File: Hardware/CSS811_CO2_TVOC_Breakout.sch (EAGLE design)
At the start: 19 parts, among them U2 CCS811PRODUCTION

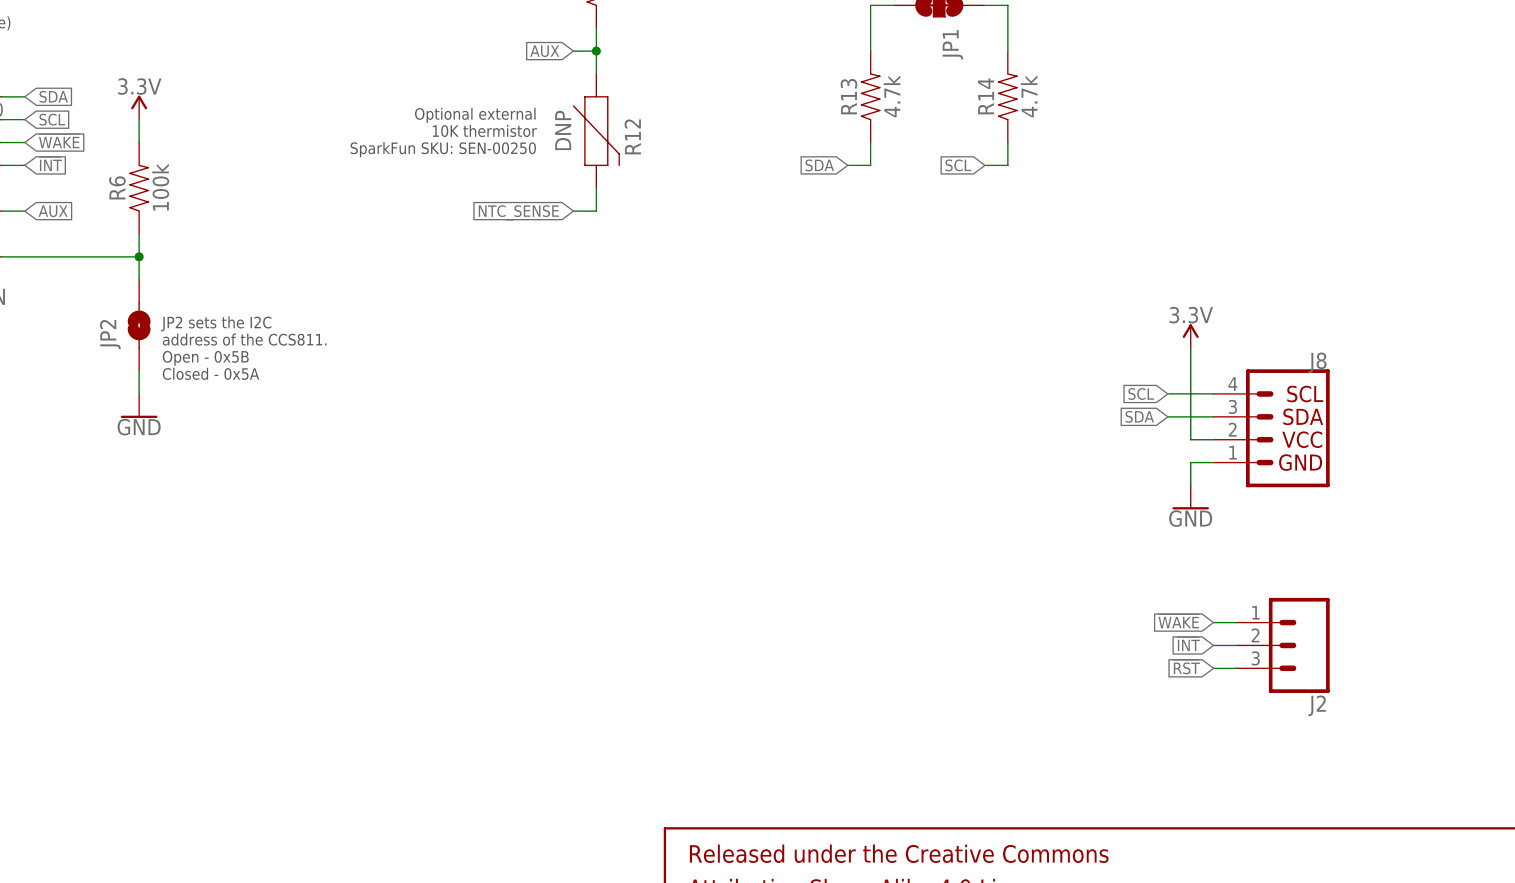
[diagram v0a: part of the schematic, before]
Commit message: Adding panel and removing extraneous files.
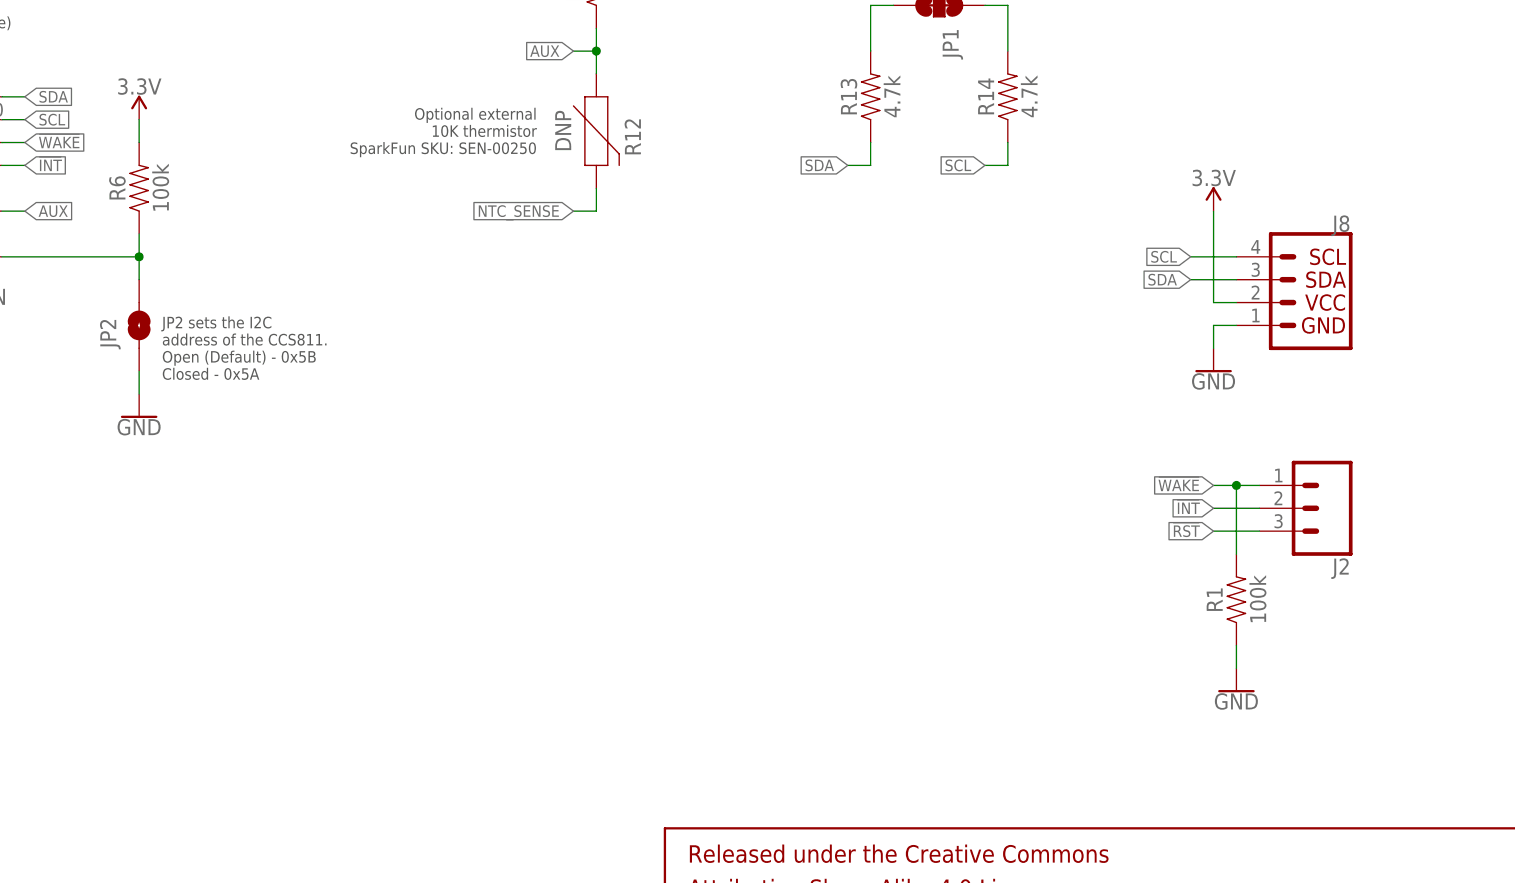
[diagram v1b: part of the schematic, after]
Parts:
- added R1: 100k, SparkFun-Resistors:100KOHM-0603-1/10W-1%
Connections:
- net !WAKE: now also R1.2
- net GND: now also R1.1
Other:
- note added: "JP2 sets the I2C address of the CCS811. Open (Default) - 0x5B Closed - 0x5A"
- note removed: "JP2 sets the I2C address of the CCS811. Open - 0x5B Closed - 0x5A"
- moved on the sheet: J2, J8
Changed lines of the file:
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@@
 <?xml version="1.0" encoding="utf-8"?>
 <!DOCTYPE eagle SYSTEM "eagle.dtd">
-<eagle version="7.5.0">
+<eagle version="7.7.0">
 <drawing>
 <settings>
@@
 <part name="J2" library="SparkFun-Connectors" deviceset="CONN_03" device="1X03_NO_SILK"/>
 <part name="U2" library="SparkX" deviceset="CCS811" device="PRODUCTION"/>
+<part name="R1" library="SparkFun-Resistors" deviceset="100KOHM" device="-0603-1/10W-1%" value="100k"/>
+<part name="GND1" library="SparkFun-PowerSymbols" deviceset="GND" device=""/>
 </parts>
 <sheets>
@@
 <text x="91.44" y="88.9" size="1.27" layer="97" align="center-left">JP2 sets the I2C
 address of the CCS811.
-Open - 0x5B
+Open (Default) - 0x5B
 Closed - 0x5A</text>
 <text x="175.26" y="132.08" size="1.27" layer="97" align="center-right">JP5 connects
@@
 <instance part="FRAME1" gate="V" x="147.32" y="0"/>
 <instance part="GND3" gate="1" x="45.72" y="93.98"/>
-<instance part="J8" gate="G$1" x="215.9" y="78.74" rot="MR0"/>
-<instance part="GND18" gate="1" x="205.74" y="71.12" rot="MR0"/>
-<instance part="SUPPLY21" gate="G$1" x="205.74" y="88.9" rot="MR0"/>
+<instance part="J8" gate="G$1" x="218.44" y="93.98" rot="MR0"/>
+<instance part="GND18" gate="1" x="208.28" y="86.36" rot="MR0"/>
+<instance part="SUPPLY21" gate="G$1" x="208.28" y="104.14" rot="MR0"/>
 <instance part="R13" gate="G$1" x="170.18" y="116.84" rot="R90"/>
 <instance part="R14" gate="G$1" x="185.42" y="116.84" rot="R90"/>
@@
 <instance part="R2" gate="G$1" x="38.1" y="119.38" rot="R90"/>
 <instance part="U$1" gate="G$1" x="132.08" y="7.62"/>
-<instance part="J2" gate="J$1" x="218.44" y="55.88" rot="R180"/>
+<instance part="J2" gate="J$1" x="220.98" y="71.12" rot="R180"/>
 <instance part="U2" gate="U1" x="60.96" y="109.22"/>
+<instance part="R1" gate="G$1" x="210.82" y="60.96" rot="R90"/>
+<instance part="GND1" gate="1" x="210.82" y="50.8" rot="MR0"/>
 </instances>
 <busses>
@@
 <segment>
 <pinref part="J8" gate="G$1" pin="1"/>
-<wire x1="208.28" y1="76.2" x2="205.74" y2="76.2" width="0.1524" layer="91"/>
-<wire x1="205.74" y1="76.2" x2="205.74" y2="73.66" width="0.1524" layer="91"/>
+<wire x1="210.82" y1="91.44" x2="208.28" y2="91.44" width="0.1524" layer="91"/>
+<wire x1="208.28" y1="91.44" x2="208.28" y2="88.9" width="0.1524" layer="91"/>
 <pinref part="GND18" gate="1" pin="GND"/>
 </segment>
@@
 <wire x1="88.9" y1="83.82" x2="88.9" y2="86.36" width="0.1524" layer="91"/>
 </segment>
+<segment>
+<pinref part="R1" gate="G$1" pin="1"/>
+<pinref part="GND1" gate="1" pin="GND"/>
+<wire x1="210.82" y1="53.34" x2="210.82" y2="55.88" width="0.1524" layer="91"/>
+</segment>
 </net>
 <net name="SCL" class="0">
 <segment>
 <pinref part="J8" gate="G$1" pin="4"/>
-<wire x1="208.28" y1="83.82" x2="203.2" y2="83.82" width="0.1524" layer="91"/>
-<label x="203.2" y="83.82" size="1.27" layer="95" rot="MR0" xref="yes"/>
+<wire x1="210.82" y1="99.06" x2="205.74" y2="99.06" width="0.1524" layer="91"/>
+<label x="205.74" y="99.06" size="1.27" layer="95" rot="MR0" xref="yes"/>
 </segment>
 <segment>
@@
 <segment>
 <pinref part="J8" gate="G$1" pin="3"/>
-<wire x1="208.28" y1="81.28" x2="203.2" y2="81.28" width="0.1524" layer="91"/>
-<label x="203.2" y="81.28" size="1.27" layer="95" rot="MR0" xref="yes"/>
+<wire x1="210.82" y1="96.52" x2="205.74" y2="96.52" width="0.1524" layer="91"/>
+<label x="205.74" y="96.52" size="1.27" layer="95" rot="MR0" xref="yes"/>
 </segment>
 <segment>
@@
 <segment>
 <pinref part="J8" gate="G$1" pin="2"/>
-<wire x1="208.28" y1="78.74" x2="205.74" y2="78.74" width="0.1524" layer="91"/>
-<wire x1="205.74" y1="78.74" x2="205.74" y2="88.9" width="0.1524" layer="91"/>
+<wire x1="210.82" y1="93.98" x2="208.28" y2="93.98" width="0.1524" layer="91"/>
+<wire x1="208.28" y1="93.98" x2="208.28" y2="104.14" width="0.1524" layer="91"/>
 <pinref part="SUPPLY21" gate="G$1" pin="3.3V"/>
 </segment>
@@
 </segment>
 <segment>
-<wire x1="210.82" y1="53.34" x2="208.28" y2="53.34" width="0.1524" layer="91"/>
-<label x="208.28" y="53.34" size="1.27" layer="95" rot="R180" xref="yes"/>
+<wire x1="213.36" y1="68.58" x2="208.28" y2="68.58" width="0.1524" layer="91"/>
+<label x="208.28" y="68.58" size="1.27" layer="95" rot="R180" xref="yes"/>
 <pinref part="J2" gate="J$1" pin="3"/>
 </segment>
@@
 </segment>
 <segment>
-<wire x1="210.82" y1="55.88" x2="208.28" y2="55.88" width="0.1524" layer="91"/>
-<label x="208.28" y="55.88" size="1.27" layer="95" rot="R180" xref="yes"/>
+<wire x1="213.36" y1="71.12" x2="208.28" y2="71.12" width="0.1524" layer="91"/>
+<label x="208.28" y="71.12" size="1.27" layer="95" rot="R180" xref="yes"/>
 <pinref part="J2" gate="J$1" pin="2"/>
 </segment>
@@
 </segment>
 <segment>
-<wire x1="210.82" y1="58.42" x2="208.28" y2="58.42" width="0.1524" layer="91"/>
-<label x="208.28" y="58.42" size="1.27" layer="95" rot="R180" xref="yes"/>
+<wire x1="213.36" y1="73.66" x2="210.82" y2="73.66" width="0.1524" layer="91"/>
+<label x="208.28" y="73.66" size="1.27" layer="95" rot="R180" xref="yes"/>
 <pinref part="J2" gate="J$1" pin="1"/>
-</segment>
-</net>
+<pinref part="R1" gate="G$1" pin="2"/>
+<wire x1="210.82" y1="73.66" x2="208.28" y2="73.66" width="0.1524" layer="91"/>
+<wire x1="210.82" y1="66.04" x2="210.82" y2="73.66" width="0.1524" layer="91"/>
+<junction x="210.82" y="73.66"/>
+</segment>
+</net>

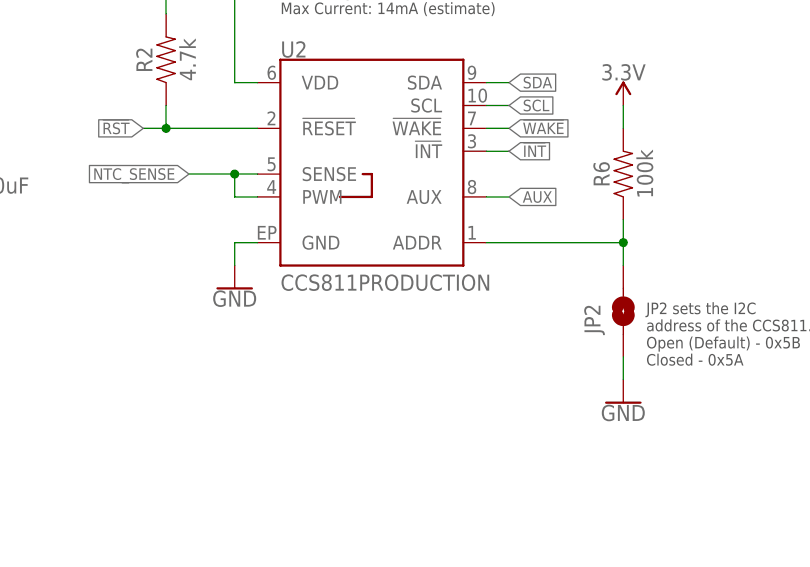
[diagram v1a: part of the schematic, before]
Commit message: Removing WAKE pin control to make examples simplier
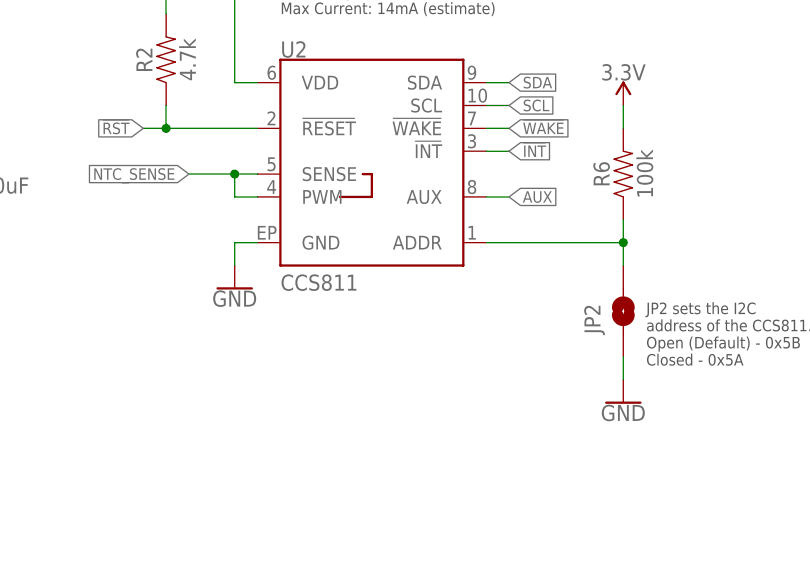
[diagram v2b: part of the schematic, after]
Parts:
- U2: value CCS811PRODUCTION -> CCS811
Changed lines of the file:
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@@
 <part name="U$1" library="SparkX" deviceset="SPARKX-LOGO" device="3"/>
 <part name="J2" library="SparkFun-Connectors" deviceset="CONN_03" device="1X03_NO_SILK"/>
-<part name="U2" library="SparkX" deviceset="CCS811" device="PRODUCTION"/>
+<part name="U2" library="SparkX" deviceset="CCS811" device="PRODUCTION" value="CCS811"/>
 <part name="R1" library="SparkFun-Resistors" deviceset="100KOHM" device="-0603-1/10W-1%" value="100k"/>
 <part name="GND1" library="SparkFun-PowerSymbols" deviceset="GND" device=""/>

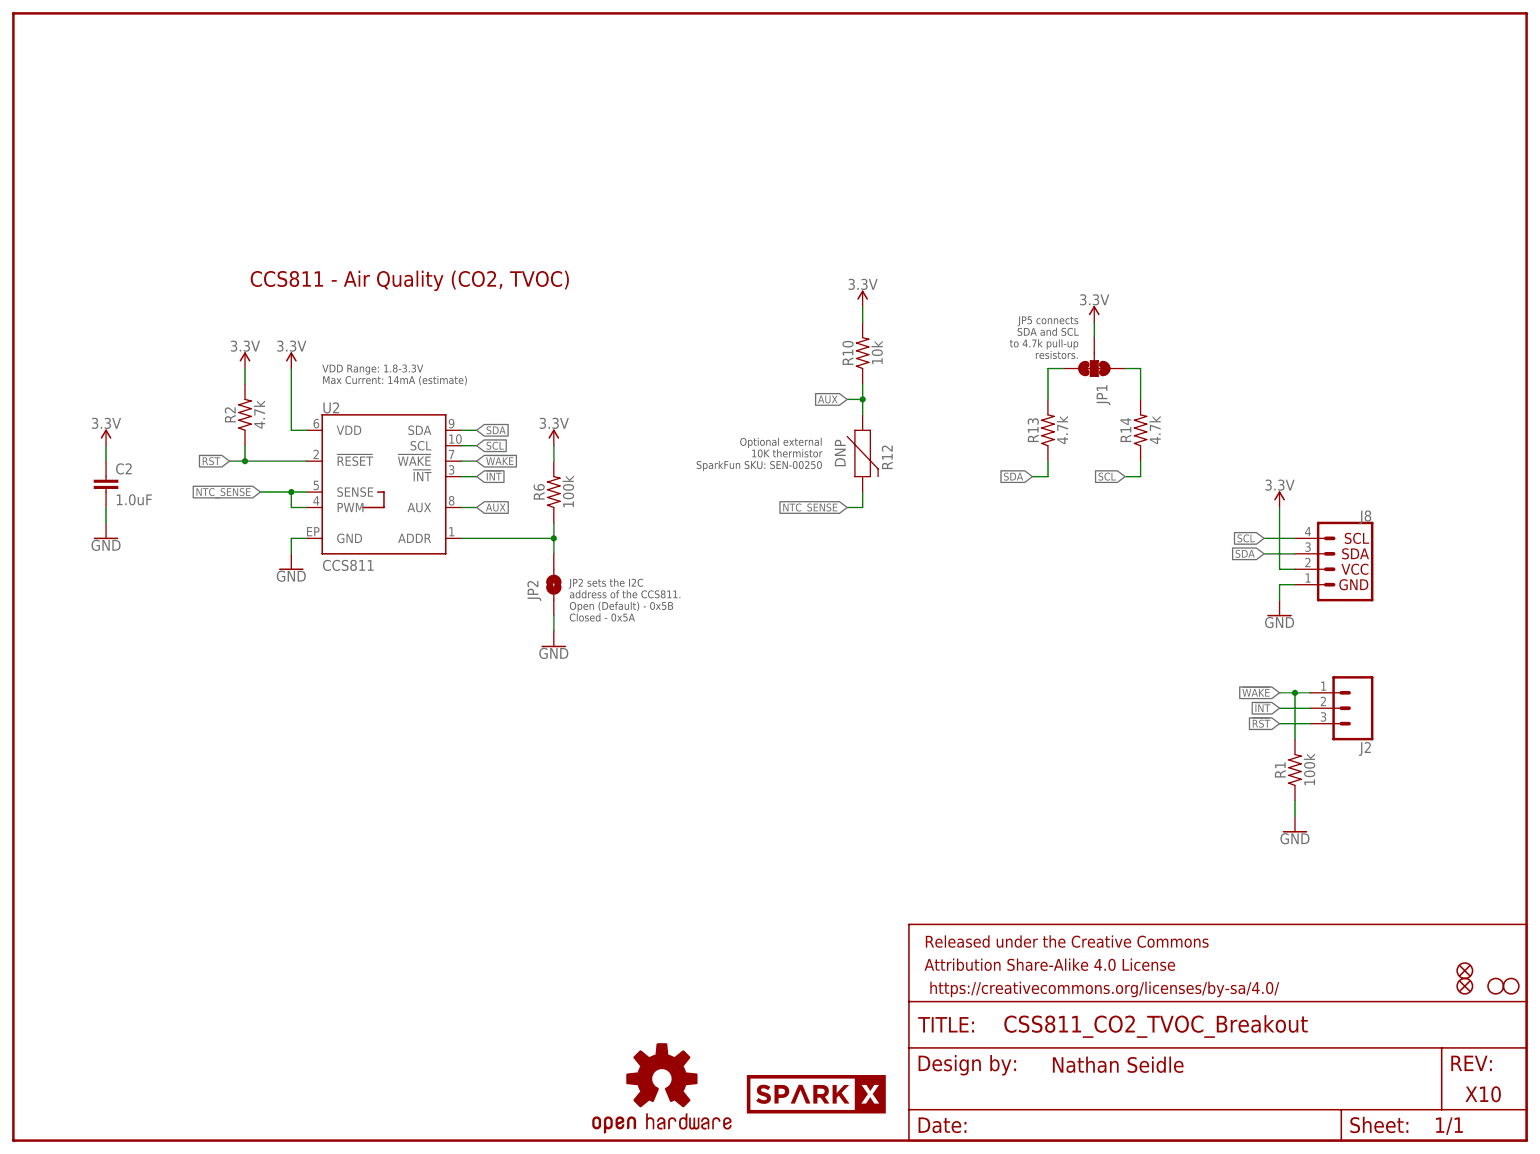
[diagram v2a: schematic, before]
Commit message: Added temp library of new parts, added proper gitignore/gitattributes, switched sparkfun logo in for sparkx logo, cleaned up schematic, changed version number to v10
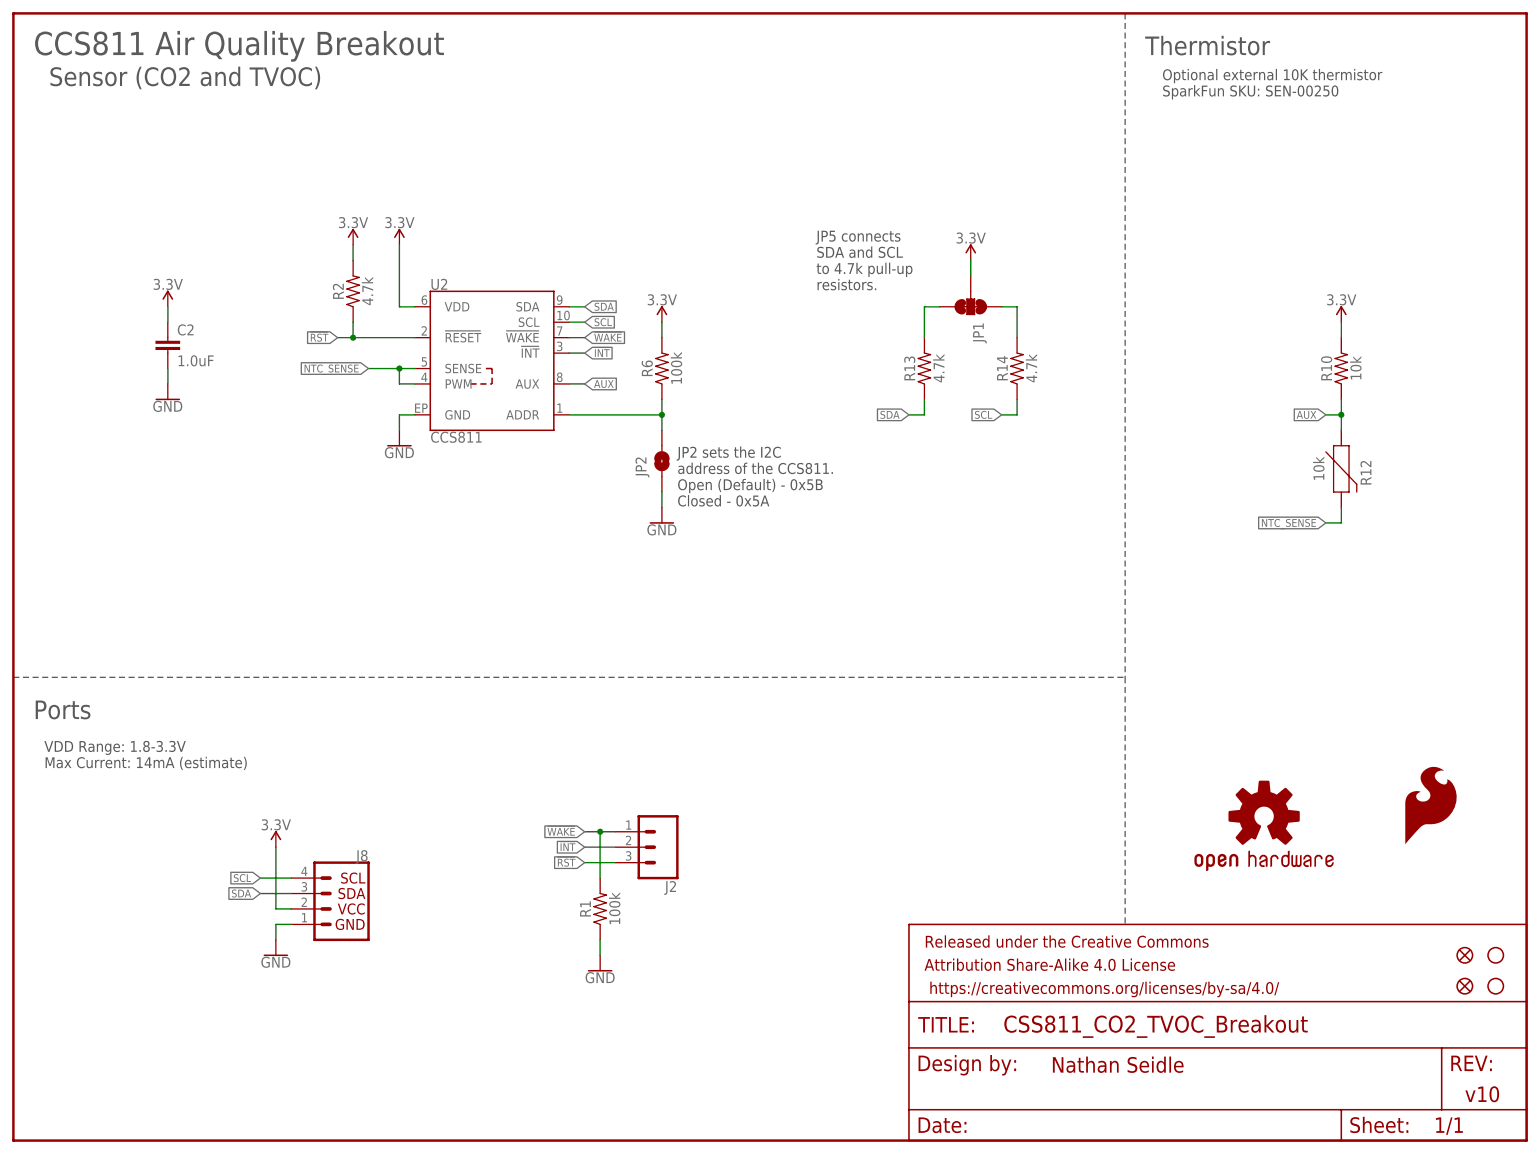
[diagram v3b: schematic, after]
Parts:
- removed U$1: SPARKX-LOGO3, SparkX:SPARKX-LOGO3
- added LOGO1: SFE_LOGO_FLAME.2_INCH, SparkFun-Aesthetics:SFE_LOGO_FLAME.2_INCH
- R12: value DNP -> 10k; device esp32-environ-monitor-temp:NTC-THERMISTOR-AXIAL-0.1 -> CCS811_Breakout_Temp:NTC-THERMISTOR-AXIAL-0.1
- U2: device SparkX:CCS811PRODUCTION -> CCS811_Breakout_Temp:CCS811
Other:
- note added: "CCS811 Air Quality Breakout"
- note added: "Ports"
- note added: "Sensor (CO2 and TVOC)"
- note added: "Thermistor"
- note added: "v10"
- note removed: "CCS811 - Air Quality (CO2, TVOC)"
- note removed: "X10"
- moved on the sheet: C2, J2, J8, JP1, JP2, R1, R10, R12, R13, R14, R2, R6
